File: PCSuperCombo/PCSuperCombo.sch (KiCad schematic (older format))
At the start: 38 parts, among them J1 IDE_CONNECTOR, J2 CF Adapter Power, J3 Bus_ISA_8bit, J4 LED, SW1 SW_DIP_x10, U1 BIOS FLASH, U2 74HCT245, U3 ATF/GAL16V8x-15, U4 DS1315, U5 AS6C1/4008-55PCN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

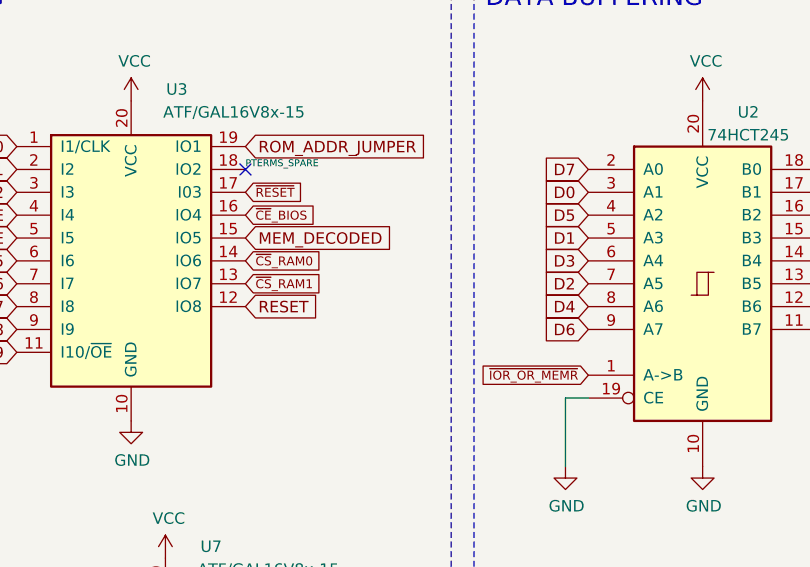
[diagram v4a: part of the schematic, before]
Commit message: PCSuperCombo: Add memory logic.
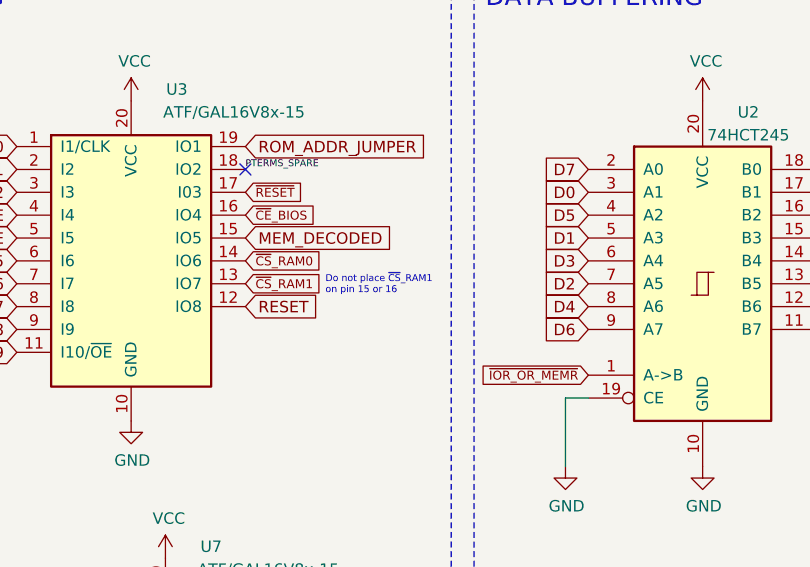
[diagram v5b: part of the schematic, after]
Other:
- note added: "Do not place ~CS~_RAM1\non pin 15 or 16"

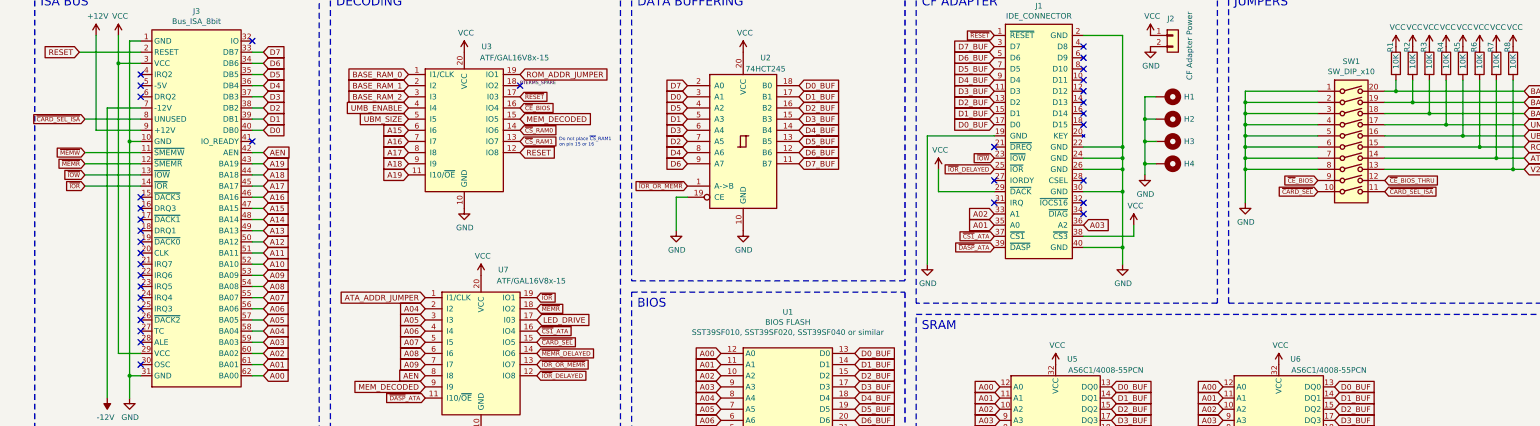
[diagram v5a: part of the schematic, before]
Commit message: PCSuperCombo: Remove CARD_SEL output from GAL logic. We are already generating this signal to set the direction of the '245 on the board.
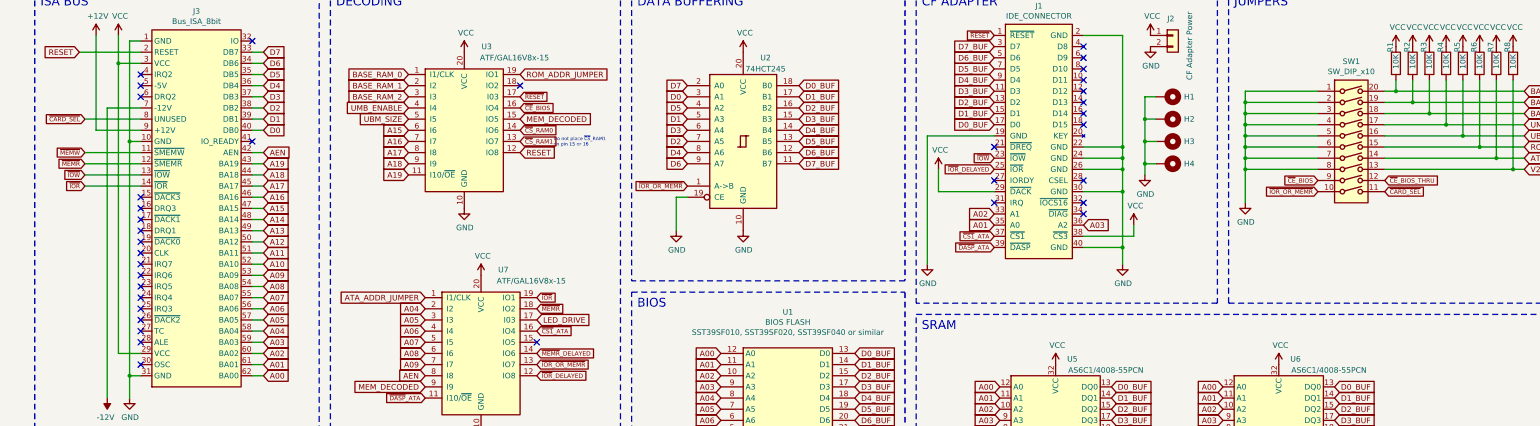
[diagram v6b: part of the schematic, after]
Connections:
- net ~CARD_SEL_ISA is gone; now on net ~CARD_SEL: J3.8 (UNUSED), SW1.11
- net ~CARD_SEL: no longer SW1.10, U7.15 (IO5)
- net ~IOR_OR_MEMR: now also SW1.10
- net PTERMS_SPARE: no longer names the net of U3.18 (IO2)
- no-connect marks 35 -> 36
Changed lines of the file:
@@
 Text GLabel 4900 1600 2    39   Input ~ 0
 ~CE~_BIOS
-Text GLabel 5050 4000 2    39   Input ~ 0
-~IOR~_DELAYED
 Text GLabel 2600 3400 2    50   Input ~ 0
 A06
@@
 	1    0    0    -1
 $EndComp
-Text GLabel 5050 3900 2    39   Input ~ 0
-~IOR_OR_MEMR
 Text GLabel 4900 1500 2    39   Input ~ 0
 ~RESET
@@
 Wire Wire Line
 	10500 1700 10500 1900
-Text GLabel 5050 3800 2    39   Input ~ 0
-~MEMR~_DELAYED
 $Comp
 L power:GND #PWR0134
@@
 	1    0    0    -1
 $EndComp
-Text GLabel 12050 2350 0    39   Input ~ 0
+Text GLabel 12650 2350 2    39   Input ~ 0
 ~CARD_SEL
-Text GLabel 12650 2350 2    39   Input ~ 0
-~CARD_SEL_ISA
 Text GLabel 1000 1700 0    39   Input ~ 0
-~CARD_SEL_ISA
+~CARD_SEL
 Wire Wire Line
 	1500 1700 1000 1700
@@
 Text GLabel 6700 6000 0    39   Input ~ 0
 ~CE~_BIOS_THRU
-Text GLabel 5050 3700 2    39   Input ~ 0
-~CARD_SEL
 Text GLabel 3900 1500 0    50   Input ~ 0
 BASE_RAM_2
@@
 Text GLabel 4050 3300 0    50   Input ~ 0
 ATA_ADDR_JUMPER
-Text GLabel 4900 1700 2    50   Input ~ 0
-MEM_DECODED
-Text GLabel 4050 4100 0    50   Input ~ 0
-MEM_DECODED
 $Comp
 L power:VCC #PWR01
@@
 	6900 7550 6900 7650
 NoConn ~ 4900 1400
-Text Label 4900 1400 0    30   ~ 0
-PTERMS_SPARE
 Text GLabel 4900 1300 2    50   Input ~ 0
 ROM_ADDR_JUMPER
@@
 	1    0    0    -1
 $EndComp
-Text Notes 5250 1950 0    30   ~ 0
+Text Notes 5200 1950 0    30   ~ 0
 Do not place ~CS~_RAM1\non pin 15 or 16
+NoConn ~ 5050 3700
+Text GLabel 12050 2350 0    39   Input ~ 0
+~IOR_OR_MEMR
+Text GLabel 4900 1700 2    50   Input ~ 0
+MEM_DECODED
+Text GLabel 4050 4100 0    50   Input ~ 0
+MEM_DECODED
+Text GLabel 5050 3800 2    39   Input ~ 0
+~MEMR~_DELAYED
+Text GLabel 5050 3900 2    39   Input ~ 0
+~IOR_OR_MEMR
+Text GLabel 5050 4000 2    39   Input ~ 0
+~IOR~_DELAYED
 $EndSCHEMATC

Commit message: PCSuperCombo: Shuffle some GAL logic around so now there is enough room in the logic to add a single UART jumper / decode.
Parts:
- added R9: 10K, Resistor_SMD:R_1206_3216Metric, symbol Device:R
- SW1: value SW_DIP_x10 -> Options; footprint Button_Switch_THT:SW_DIP_SPSTx10_Slide_9.78x27.58mm_W7.62mm_P2.54mm -> Button_Switch_THT:SW_DIP_SPSTx12_Slide_9.78x32.66mm_W7.62mm_P2.54mm; symbol Switch:SW_DIP_x10 -> Switch:SW_DIP_x12
- renumbered R9 to R11
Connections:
- net ATA_ADDR_JUMPER: now also SW1.18; no longer SW1.14
- net BASE_RAM_0: now also SW1.24; no longer SW1.20
- net BASE_RAM_1: now also SW1.23; no longer SW1.19
- net BASE_RAM_2: now also SW1.22; no longer SW1.18
- net GND: now also SW1.9
- net RESET: now also U7.14 (IO6); no longer U3.12 (IO8)
- net ROM_ADDR_JUMPER: now also SW1.19; no longer SW1.15
- net V20_JUMPER: now also SW1.16, R9.2; no longer R8.2, SW1.13
- net VCC: now also R9.1
- net ~CARD_SEL: now also SW1.13; no longer SW1.11
- net ~CE~_BIOS: now also SW1.11; no longer SW1.9
- net ~CE~_BIOS_THRU: now also SW1.14; no longer SW1.12
- net ~IOR_OR_MEMR: now also SW1.12, U3.12 (IO8); no longer SW1.10, U7.13 (IO7)
- net ~IOR~_DELAYED: now also U3.18 (IO2); no longer U7.12 (IO8)
- net ~MEMR~_DELAYED: now also U3.17 (I03); no longer U7.14 (IO6)
- net ~RESET: now also U7.15 (IO5); no longer U3.17 (I03)
- net MEM_DECODED renamed COM1_ENABLE
- net COM1_ENABLE: now also R8.2, SW1.17; no longer U3.15 (IO5)
- net UBM_SIZE renamed UMB_SIZE_1
- net UMB_SIZE_1: now also SW1.20; no longer SW1.16
- net UMB_ENABLE renamed UMB_SIZE_0
- net UMB_SIZE_0: now also SW1.21; no longer SW1.17
- new net IO_DECODED: U3.15 (IO5), U7.12 (IO8)
- new net ~CS~_COM1: U7.13 (IO7)
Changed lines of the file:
@@
 Wire Wire Line
 	2500 2600 2600 2600
-Text GLabel 4900 2000 2    50   Input ~ 0
+Text GLabel 5050 3800 2    50   Input ~ 0
 RESET
 Text GLabel 5050 3400 2    39   Input ~ 0
@@
 	1    0    0    -1
 $EndComp
-Text GLabel 4900 1500 2    39   Input ~ 0
+Text GLabel 5050 3700 2    39   Input ~ 0
 ~RESET
 Text GLabel 5050 3300 2    39   Input ~ 0
@@
 	1    0    0    -1
 $EndComp
-Text GLabel 13900 2050 2    50   Input ~ 0
+Text GLabel 14050 2050 2    50   Input ~ 0
 ATA_ADDR_JUMPER
-Text GLabel 13900 1950 2    50   Input ~ 0
+Text GLabel 14050 1950 2    50   Input ~ 0
 ROM_ADDR_JUMPER
-Text GLabel 12050 2250 0    39   Input ~ 0
+Text GLabel 12050 2450 0    39   Input ~ 0
 ~CE~_BIOS
-Text GLabel 12650 2250 2    39   Input ~ 0
+Text GLabel 12650 2450 2    39   Input ~ 0
 ~CE~_BIOS_THRU
 $Comp
@@
 	1    0    0    -1
 $EndComp
-Text GLabel 13900 2150 2    50   Input ~ 0
+Text GLabel 14050 2250 2    50   Input ~ 0
 V20_JUMPER
 Text GLabel 6700 5400 0    50   Input ~ 0
@@
 128Kx8 for UMB only\nwhen all of 512Kx8\nneeded for base.
 $Comp
-L Switch:SW_DIP_x10 SW1
+L Switch:SW_DIP_x12 SW1
 U 1 1 61692810
-P 12350 1950
-F 0 "SW1" H 12350 2717 50  0000 C CNN
-F 1 "SW_DIP_x10" H 12350 2626 50  0000 C CNN
-F 2 "Button_Switch_THT:SW_DIP_SPSTx10_Slide_9.78x27.58mm_W7.62mm_P2.54mm" H 12350 1950 50  0001 C CNN
-F 3 "~" H 12350 1950 50  0001 C CNN
-	1    12350 1950
-	1    0    0    -1
-$EndComp
-Text GLabel 12650 2350 2    39   Input ~ 0
+P 12350 2050
+F 0 "SW1" H 12350 2817 50  0000 C CNN
+F 1 "Options" H 12350 1400 50  0000 C CNN
+F 2 "Button_Switch_THT:SW_DIP_SPSTx12_Slide_9.78x32.66mm_W7.62mm_P2.54mm" H 12350 2050 50  0001 C CNN
+F 3 "~" H 12350 2050 50  0001 C CNN
+	1    12350 2050
+	1    0    0    -1
+$EndComp
+Text GLabel 12650 2550 2    39   Input ~ 0
 ~CARD_SEL
 Text GLabel 1000 1700 0    39   Input ~ 0
@@
 Wire Wire Line
 	1500 1700 1000 1700
-Text GLabel 13900 1450 2    50   Input ~ 0
+Text GLabel 14050 1450 2    50   Input ~ 0
 BASE_RAM_0
-Text GLabel 13900 1550 2    50   Input ~ 0
+Text GLabel 14050 1550 2    50   Input ~ 0
 BASE_RAM_1
-Text GLabel 13900 1650 2    50   Input ~ 0
+Text GLabel 14050 1650 2    50   Input ~ 0
 BASE_RAM_2
-Text GLabel 13900 1750 2    50   Input ~ 0
-UMB_ENABLE
-Text GLabel 13900 1850 2    50   Input ~ 0
-UBM_SIZE
+Text GLabel 14050 1750 2    50   Input ~ 0
+UMB_SIZE_0
+Text GLabel 14050 1850 2    50   Input ~ 0
+UMB_SIZE_1
 $Comp
 L power:GND #PWR0144
@@
 Connection ~ 11400 2150
 Wire Wire Line
-	11400 2150 11400 2450
+	11400 2150 11400 2250
 $Comp
 L Device:R R1
@@
 	12650 1550 12900 1550
 Wire Wire Line
-	13900 1650 13050 1650
+	14050 1650 13050 1650
 Wire Wire Line
 	12650 1750 13200 1750
@@
 	12650 1950 13500 1950
 Wire Wire Line
-	13900 2050 13650 2050
+	14050 2050 13650 2050
 Wire Wire Line
 	12650 2150 13800 2150
@@
 Connection ~ 12750 1450
 Wire Wire Line
-	12750 1450 13900 1450
+	12750 1450 14050 1450
 Wire Wire Line
 	12900 1350 12900 1550
 Connection ~ 12900 1550
 Wire Wire Line
-	12900 1550 13900 1550
+	12900 1550 14050 1550
 Wire Wire Line
 	13050 1350 13050 1650
@@
 Connection ~ 13200 1750
 Wire Wire Line
-	13200 1750 13900 1750
+	13200 1750 14050 1750
 Wire Wire Line
 	13350 1350 13350 1850
@@
 Connection ~ 13350 1850
 Wire Wire Line
-	13350 1850 13900 1850
+	13350 1850 14050 1850
 Wire Wire Line
 	13500 1350 13500 1950
 Connection ~ 13500 1950
 Wire Wire Line
-	13500 1950 13900 1950
+	13500 1950 14050 1950
 Wire Wire Line
 	13650 1350 13650 2050
@@
 Connection ~ 13800 2150
 Wire Wire Line
-	13800 2150 13900 2150
+	13800 2150 14050 2150
 $Comp
 L power:GND #PWR0114
@@
 F 3 "" H 4550 3100 50  0001 C CNN
 	1    4550 3100
-	1    0    0    -1
-$EndComp
-$Comp
-L 00Common:GAL16V8 U7
-U 1 1 617A2256
-P 4550 3800
-F 0 "U7" H 4750 4550 50  0000 C CNN
-F 1 "ATF/GAL16V8x-15" H 5000 4450 50  0000 C CNN
-F 2 "Package_DIP:DIP-20_W7.62mm_Socket" H 4550 3800 50  0001 C CNN
-F 3 "" H 4550 3800 50  0001 C CNN
-	1    4550 3800
 	1    0    0    -1
 $EndComp
@@
 BASE_RAM_2
 Text GLabel 3900 1600 0    50   Input ~ 0
-UMB_ENABLE
+UMB_SIZE_0
 Text GLabel 3900 1700 0    50   Input ~ 0
-UBM_SIZE
+UMB_SIZE_1
 Text GLabel 4050 3300 0    50   Input ~ 0
 ATA_ADDR_JUMPER
@@
 ~DASP~_ATA
 $Comp
-L Device:R R9
+L Device:R R11
 U 1 1 617266A6
 P 6850 7750
-F 0 "R9" V 6750 7650 50  0000 L CNN
+F 0 "R11" V 6750 7650 50  0000 L CNN
 F 1 "180R" V 6950 7650 50  0000 L CNN
 F 2 "Resistor_SMD:R_1206_3216Metric" V 6780 7750 50  0001 C CNN
@@
 Wire Wire Line
 	6900 7550 6900 7650
-NoConn ~ 4900 1400
 Text GLabel 4900 1300 2    50   Input ~ 0
 ROM_ADDR_JUMPER
@@
 Text Notes 5200 1950 0    30   ~ 0
 Do not place ~CS~_RAM1\non pin 15 or 16
-NoConn ~ 5050 3700
-Text GLabel 12050 2350 0    39   Input ~ 0
+Text GLabel 12050 2550 0    39   Input ~ 0
 ~IOR_OR_MEMR
+Text GLabel 5050 4000 2    50   Input ~ 0
+IO_DECODED
+Text GLabel 4900 1500 2    39   Input ~ 0
+~MEMR~_DELAYED
+Text GLabel 4900 2000 2    39   Input ~ 0
+~IOR_OR_MEMR
+Text GLabel 4900 1400 2    39   Input ~ 0
+~IOR~_DELAYED
 Text GLabel 4900 1700 2    50   Input ~ 0
-MEM_DECODED
+IO_DECODED
+$Comp
+L 00Common:GAL16V8 U7
+U 1 1 617A2256
+P 4550 3800
+F 0 "U7" H 4750 4550 50  0000 C CNN
+F 1 "ATF/GAL16V8x-15" H 5000 4450 50  0000 C CNN
+F 2 "Package_DIP:DIP-20_W7.62mm_Socket" H 4550 3800 50  0001 C CNN
+F 3 "" H 4550 3800 50  0001 C CNN
+	1    4550 3800
+	1    0    0    -1
+$EndComp
+NoConn ~ 12050 2350
+NoConn ~ 12650 2350
+$Comp
+L power:VCC #PWR0157
+U 1 1 6166B6AD
+P 13950 1050
+F 0 "#PWR0157" H 13950 900 50  0001 C CNN
+F 1 "VCC" H 13965 1223 50  0000 C CNN
+F 2 "" H 13950 1050 50  0001 C CNN
+F 3 "" H 13950 1050 50  0001 C CNN
+	1    13950 1050
+	1    0    0    -1
+$EndComp
+$Comp
+L Device:R R9
+U 1 1 6166BEF0
+P 13950 1200
+F 0 "R9" V 13900 1300 50  0000 L CNN
+F 1 "10K" V 13950 1150 50  0000 L CNN
+F 2 "Resistor_SMD:R_1206_3216Metric" V 13880 1200 50  0001 C CNN
+F 3 "~" H 13950 1200 50  0001 C CNN
+F 4 "C17902" H 13950 1200 50  0001 C CNN "LCSC"
+	1    13950 1200
+	1    0    0    -1
+$EndComp
+Wire Wire Line
+	12650 2250 13950 2250
+Wire Wire Line
+	13950 1350 13950 2250
+Connection ~ 13950 2250
+Wire Wire Line
+	13950 2250 14050 2250
+Wire Wire Line
+	12050 2250 11400 2250
+Connection ~ 11400 2250
+Wire Wire Line
+	11400 2250 11400 2450
+Text GLabel 14050 2150 2    50   Input ~ 0
+COM1_ENABLE
 Text GLabel 4050 4100 0    50   Input ~ 0
-MEM_DECODED
-Text GLabel 5050 3800 2    39   Input ~ 0
-~MEMR~_DELAYED
+COM1_ENABLE
 Text GLabel 5050 3900 2    39   Input ~ 0
-~IOR_OR_MEMR
-Text GLabel 5050 4000 2    39   Input ~ 0
-~IOR~_DELAYED
+~CS~_COM1
 $EndSCHEMATC

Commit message: Initial work on addiing serial to PCSuperCombo.
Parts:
- removed H4: MountingHole_Pad, MountingHole:MountingHole_3.5mm_Pad, symbol Mechanical:MountingHole_Pad
- added CN1: DB9 Male, Connector_Dsub:DSUB-9_Male_Horizontal_P2.77x2.84mm_EdgePinOffset7.70mm_Housed_MountingHolesOffset9.12mm, symbol Connector:DB9_Male
- added U10: 1.8432 MHz, Oscillator:Oscillator_SMD_SeikoEpson_SG8002CA-4Pin_7.0x5.0mm, symbol Oscillator:SG-7050CAN
- added U8: 16C550, Package_QFP:LQFP-48_7x7mm_P0.5mm, symbol 00Common:16550_48
- added U9: GD75232, Package_SO:SOIC-20W_7.5x12.8mm_P1.27mm, symbol Interface_UART:GD75232N
- SW1: footprint Button_Switch_THT:SW_DIP_SPSTx12_Slide_9.78x32.66mm_W7.62mm_P2.54mm -> 00Custom:SW_DIP_SPSTx12
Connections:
- net +12V: now also U9.1 (VDD)
- net -12V: now also U9.10 (VSS)
- net A00: now also U8.28 (A0)
- net A01: now also U8.27 (A1)
- net A02: now also U8.26 (A2)
- net D0: now also U8.43 (D0)
- net D1: now also U8.44 (D1)
- net D2: now also U8.45 (D2)
- net D3: now also U8.1 (NC), U8.46 (D3)
- net D4: now also U8.47 (D4), U8.48 (NC)
- net D5: now also U8.2 (D5)
- net D6: now also U8.3 (D6)
- net D7: now also U8.4 (D7)
- net GND: now also CN1.5, U10.2 (GND), U8.17 (WR), U8.18 (GND), U8.20 (RD), U8.24 (~ADS~), U9.11 (GND)
- net RESET: now also U8.25 (NC), U8.35 (MR)
- net VCC: now also U10.1 (~ST), U10.4 (VCC), U8.10 (CS1), U8.42 (VCC), U8.6 (NC), U8.9 (CS0), U9.20 (VCC)
- net ~IOR: now also U8.19 (~RD~)
- net ~IOW: now also U8.16 (~WR~)
- new net: U8.39 (~DSR~), U9.12 (RY5)
- new net: U8.32 (~RTS~), U9.13 (DA3)
- new net: U8.37 (NC), U8.7 (SIN), U9.14 (RY4)
- new net: U8.33 (~DTR~), U9.15 (DA2)
- new net: U8.36 (NC), U8.8 (SOUT), U9.16 (DA1)
- new net: U8.38 (~CTS~), U9.17 (RY3)
- new net: U8.40 (~DCD~), U9.18 (RY2)
- new net: U8.41 (~RI~), U9.19 (RY1)
- new net: U8.12 (~BAUDOUT~), U8.5 (RCLK)
- new net IRQ4: U8.30 (INTR)
- new net SER_PIN1: CN1.1, U9.3 (RA2)
- new net SER_PIN2: CN1.2, U9.7 (RA4)
- new net SER_PIN3: CN1.3, U9.5 (DY1)
- new net SER_PIN4: CN1.4, U9.6 (DY2)
- new net SER_PIN6: CN1.6, U9.9 (RA5)
- new net SER_PIN7: CN1.7, U9.8 (DY3)
- new net SER_PIN8: CN1.8, U9.4 (RA3)
- new net SER_PIN9: CN1.9, U9.2 (RA1)
- new net UART_XIN: U10.3 (OUT), U8.14 (XIN), U8.21 (NC)
- new net ~UART_CS: U8.11 (~CS2~)
- no-connect marks 36 -> 43
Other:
- note added: "Connections to N/C pins\nare to assist with routing."
- note added: "UART AND\nPORT TRANCEIVERS"
- moved on the sheet: BAT1, C1, C10, C2, C3, C4, C5, C6, C7, C8, C9, J4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
